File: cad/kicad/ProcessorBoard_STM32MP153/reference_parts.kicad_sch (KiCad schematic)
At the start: 18 parts, among them SW99901 SW_DIP_x03

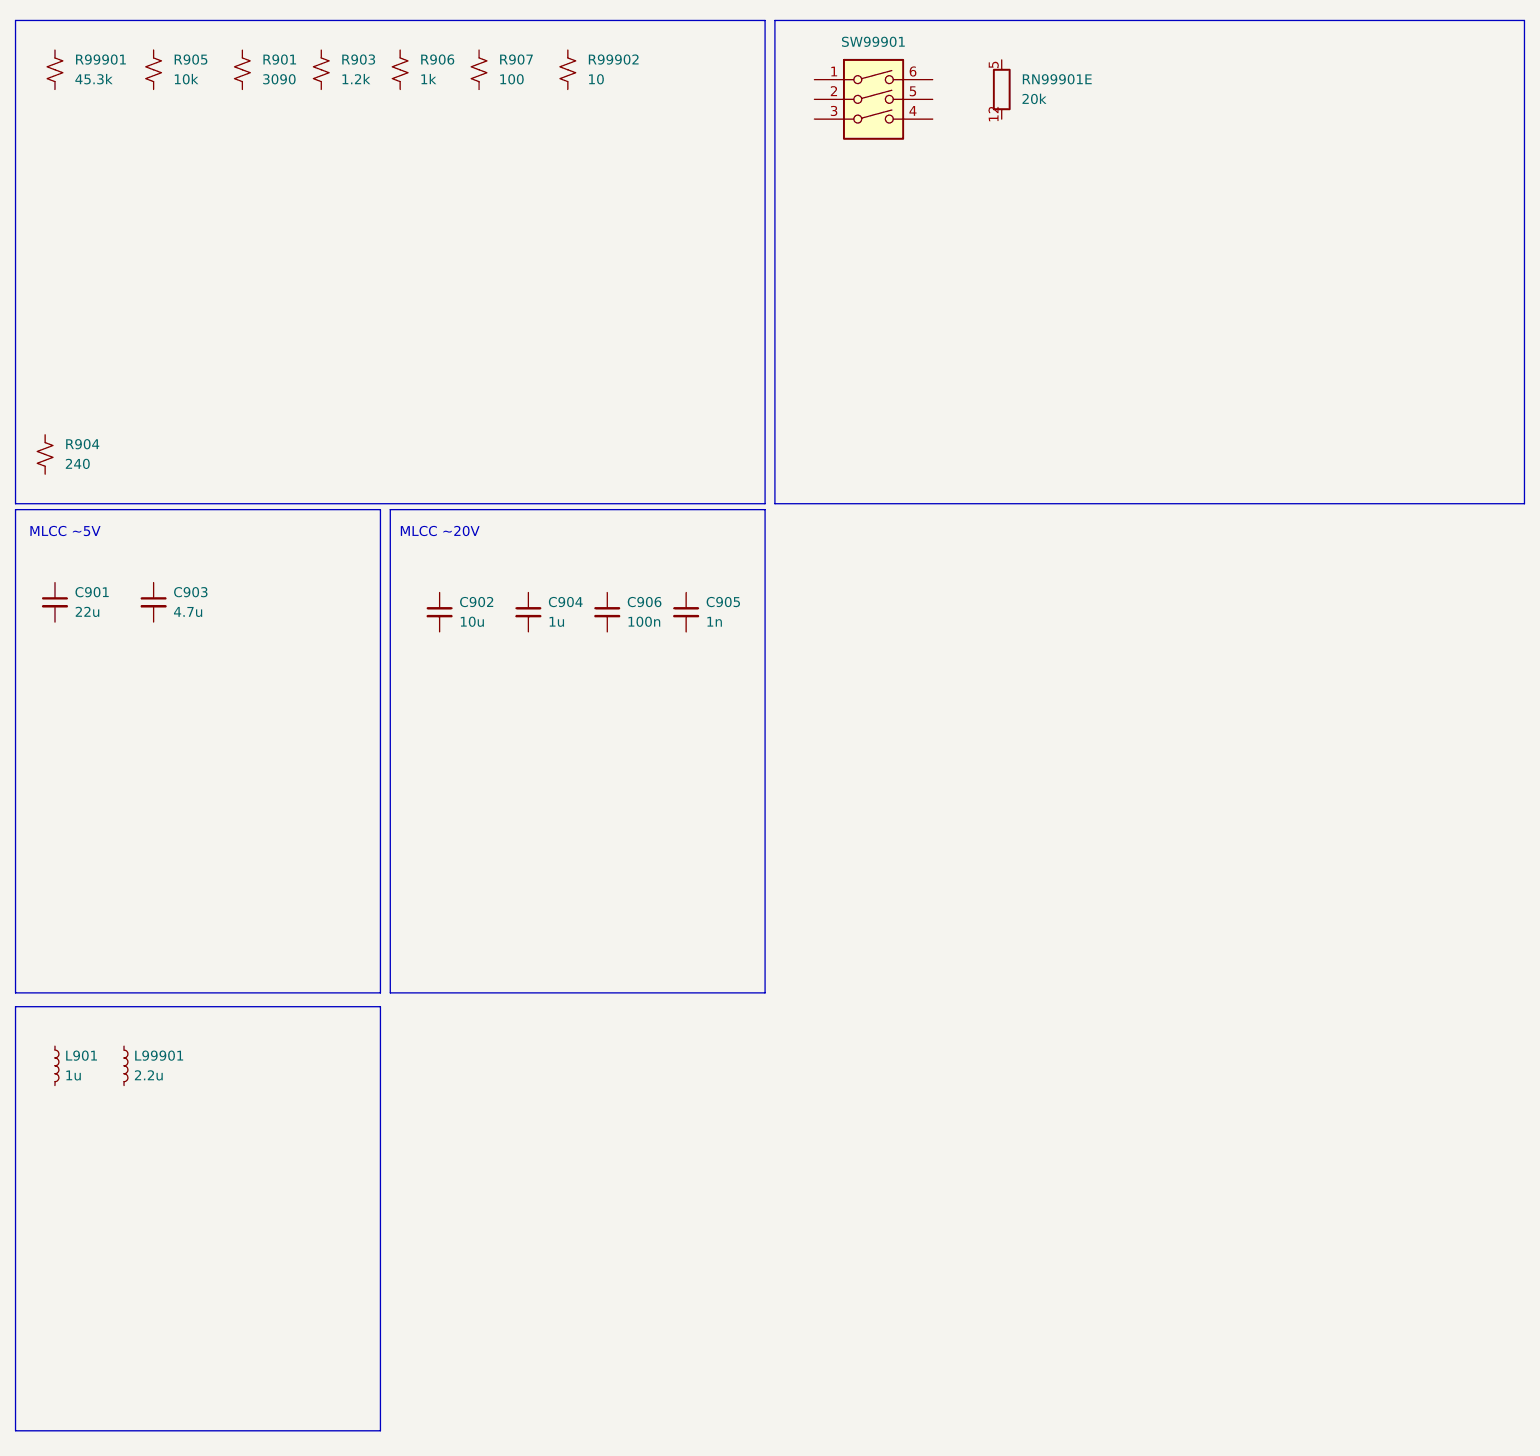
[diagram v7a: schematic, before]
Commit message: realtek bridge thing somewhat more wired
apparently the proper term for via skimping and what not is NFPR (non functional pad removal). all my homies love NFPR. so it is possible to route 0.5mm bga. still fighting the dog but at least cant bring it to another layer
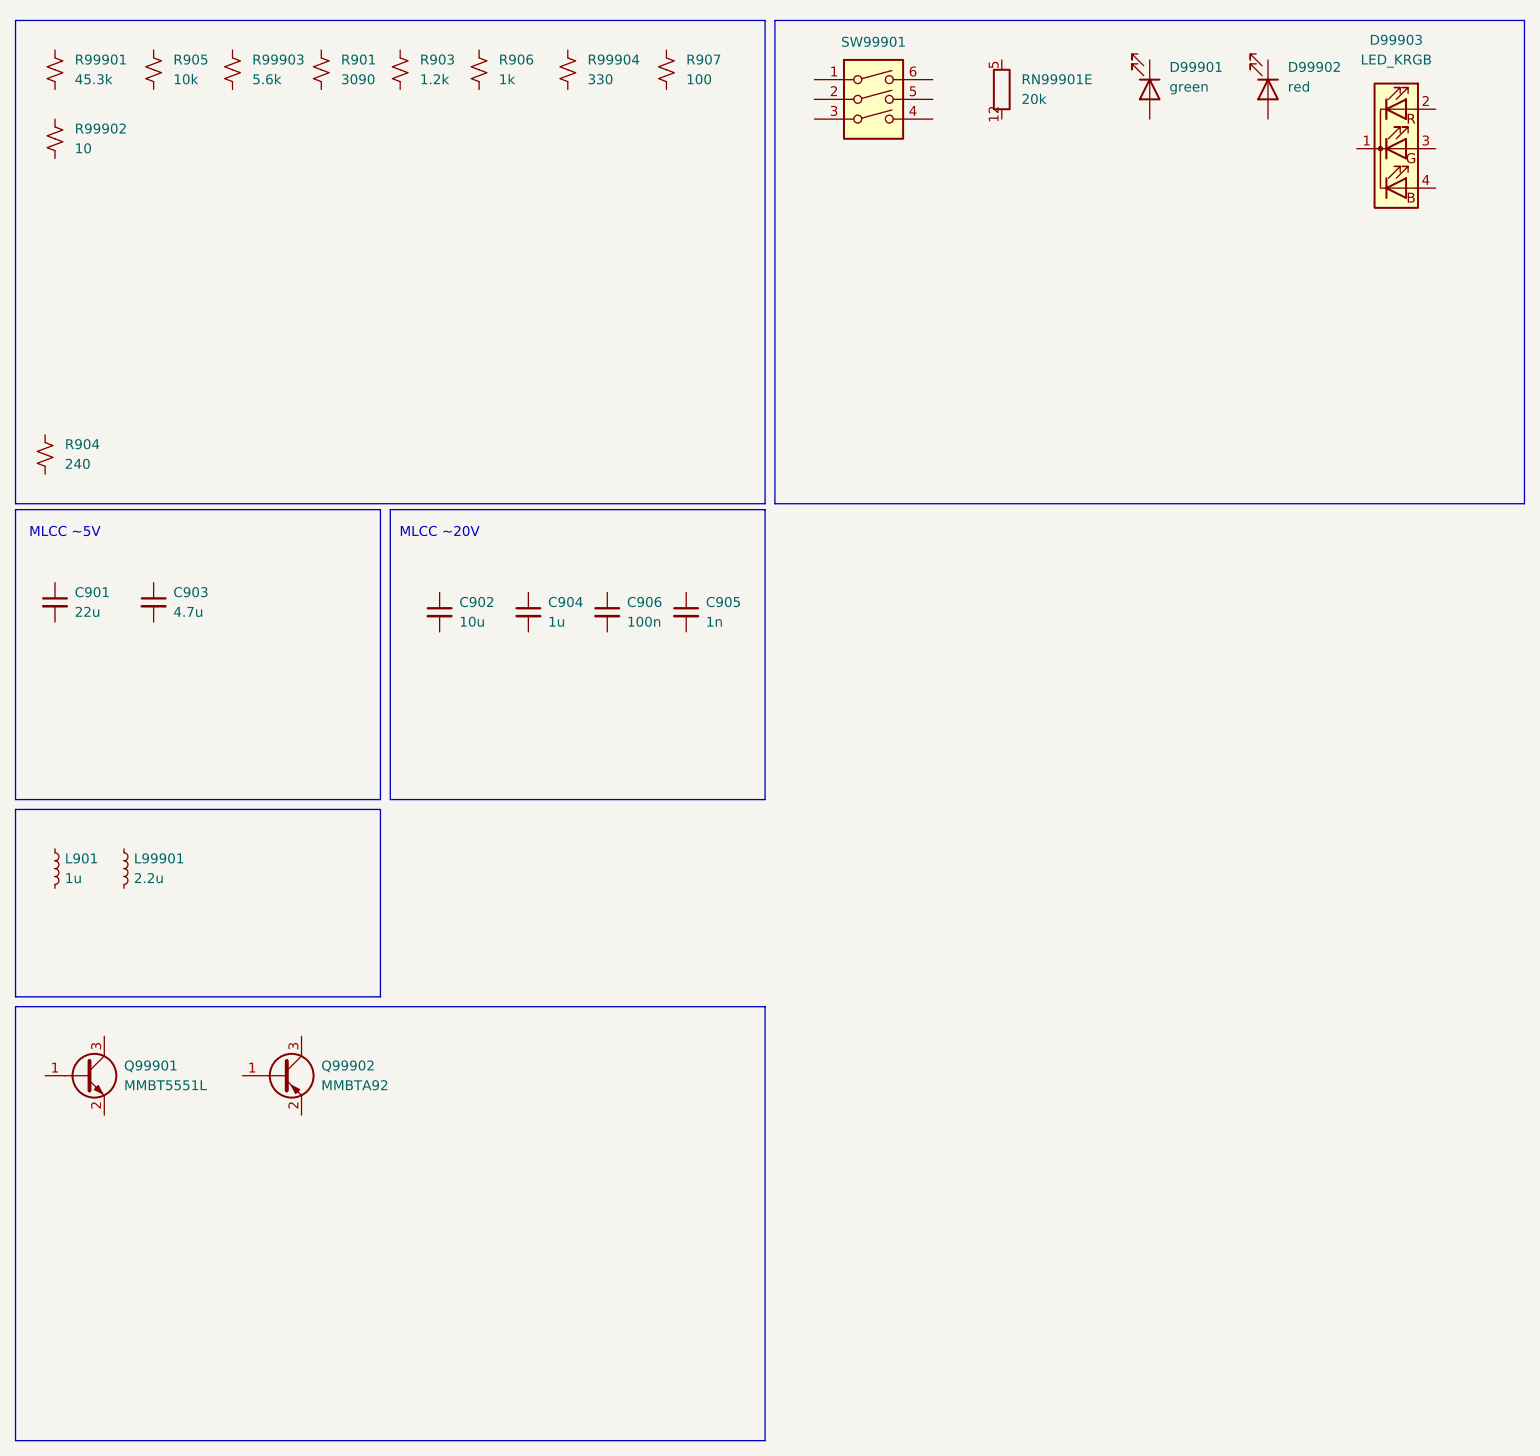
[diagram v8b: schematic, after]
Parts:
- added D99901: green, LED_SMD:LED_0603_1608Metric_Pad1.05x0.95mm_HandSolder, symbol Device:LED
- added D99902: red, LED_SMD:LED_0603_1608Metric_Pad1.05x0.95mm_HandSolder, symbol Device:LED
- added D99903: LED_KRGB, LED_SMD:LED_Cree-PLCC4_2x2mm_CW, symbol Device:LED_KRGB
- added Q99901: MMBT5551L, Package_TO_SOT_SMD:SOT-23, symbol Transistor_BJT:MMBT5551L
- added Q99902: MMBTA92, Package_TO_SOT_SMD:SOT-23, symbol Transistor_BJT:MMBTA92
- added R99903: 5.6k, Resistor_SMD:R_0805_2012Metric_Pad1.20x1.40mm_HandSolder, symbol Device:R_Small_US
- added R99904: 330, Resistor_SMD:R_0603_1608Metric_Pad0.98x0.95mm_HandSolder, symbol Device:R_Small_US
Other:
- moved on the sheet: L901, L99901, R901, R903, R906, R907, R99902
